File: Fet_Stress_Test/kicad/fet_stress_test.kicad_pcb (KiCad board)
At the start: 2 copper layers, 45 x 121.8 mm, 20 parts, among them Q1 MMBT3904

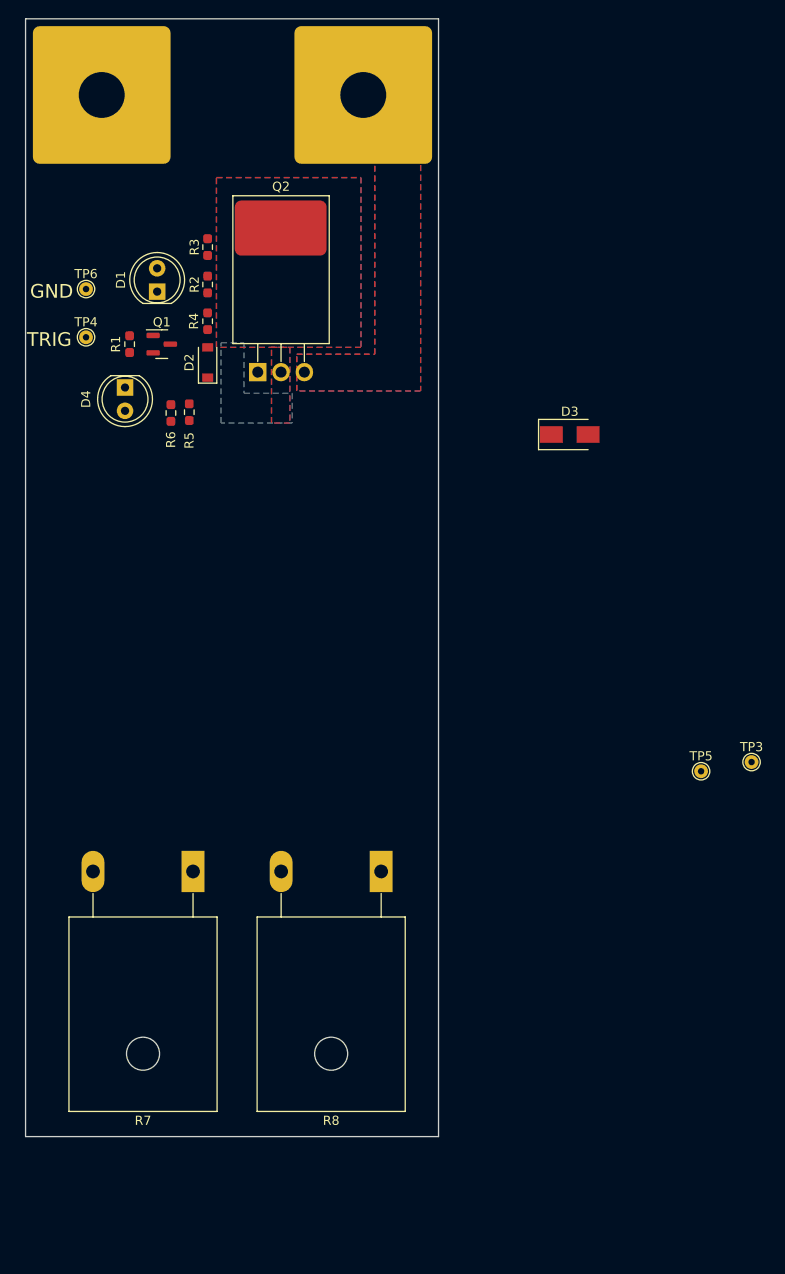
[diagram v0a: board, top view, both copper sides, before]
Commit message: Finsihed stress test pcb and generated gerbes
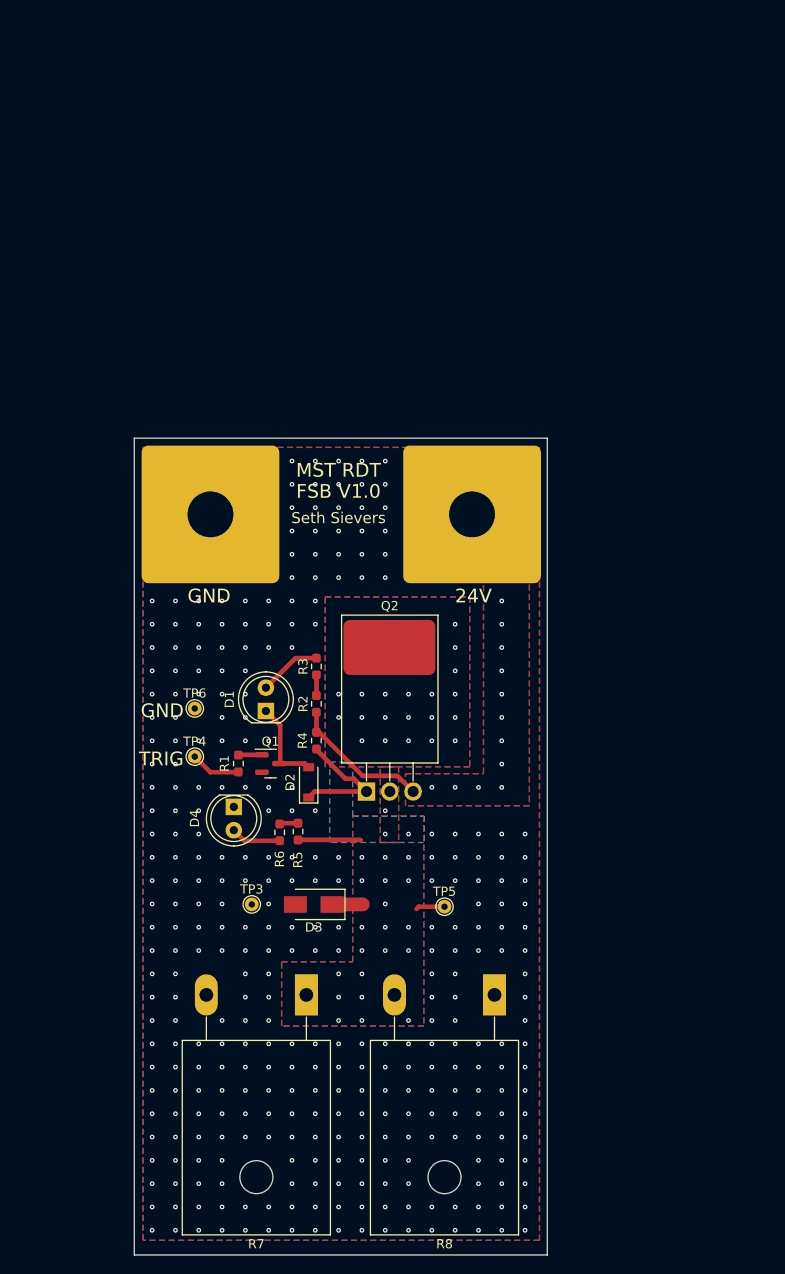
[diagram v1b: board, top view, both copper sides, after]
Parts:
- moved D3 58.3 mm to (119.1, 110.7), turned to 180 degrees
- moved TP3 56.6 mm to (112.3, 110.7)
- moved Q1 47.2 mm to (114.4, 95.3)
- moved R1 47.2 mm to (110.9, 95.3)
- moved R2 47.2 mm to (119.4, 88.8)
- moved R4 47.2 mm to (119.4, 92.8)
- moved R6 47.2 mm to (115.4, 102.8)
- moved TP4 47.2 mm to (106.1, 94.6)
- moved TP6 47.2 mm to (106.1, 89.3)
- moved D1 47.2 mm to (113.9, 89.6)
- moved D4 47.2 mm to (110.4, 100.1)
- moved Q2 47.2 mm to (124.8, 98.4)
- moved R3 47.2 mm to (119.4, 84.8)
- moved R5 47.2 mm to (117.4, 102.8)
- moved TP1 47.2 mm to (107.8, 68.2)
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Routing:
- net Net-(D2-Pad1): track 0.00 -> 15.7 mm
- net /24V: track 0.00 -> 15.4 mm, vias 0 -> 12
- net /OUTPUT: track 0.00 -> 13.3 mm, vias 0 -> 43
- net Net-(D1-Pad1): track 0.00 -> 9.81 mm
- net Net-(D1-Pad2): track 0.00 -> 6.83 mm
- net Net-(D4-Pad2): track 0.00 -> 5.48 mm
- net Net-(R1-Pad2): track 0.00 -> 5.47 mm
- net Net-(Q1-Pad1): track 0.00 -> 2.58 mm
- net Net-(R2-Pad2): track 0.00 -> 2.25 mm
- net Net-(R5-Pad2): track 0.00 -> 2.04 mm
- net GND: vias 0 -> 327
- added copper zone on B.Cu, net GND
- added copper zone on F.Cu, net GND
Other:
- board size 45 x 121.8 mm -> 45 x 89 mm
- board text added: "24V"
- board text added: "FSB V1.0"
- board text added: "MST RDT"
- board text added: "Seth Sievers"

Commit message: Finalized footprints and regenerated gerbers, added BOM
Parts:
- added J1: GX_16-2, DOM:GX_16-2, F.Cu at (123.0, 133.1)
- added J2: GX_16-3, DOM:GX_16-3, F.Cu at (111.0, 133.0)
- added J3: GX_16-4, DOM:GX_16-4, F.Cu at (134.0, 132.4)
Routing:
- net GND: vias 327 -> 275

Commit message: small pcb update
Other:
- board text added: "OUT"
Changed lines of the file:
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@@
   )
   (gr_rect (start 99.55 59.9) (end 144.55 148.9) (layer "Edge.Cuts") (width 0.1) (fill none))
+  (gr_text "OUT" (at 137.2 111) (layer "F.SilkS")
+    (effects (font (size 1.5 1.5) (thickness 0.3)))
+  )
   (gr_text "TRIG" (at 102.5 94.85) (layer "F.SilkS")
     (effects (font (size 1.5 1.5) (thickness 0.3)))
@@
     (effects (font (size 1.5 1.5) (thickness 0.3)))
   )
+  (gr_text "GND" (at 108.7 110.7) (layer "F.SilkS")
+    (effects (font (size 1.5 1.5) (thickness 0.3)))
+  )
